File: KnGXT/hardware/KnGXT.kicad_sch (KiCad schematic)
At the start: 134 parts, among them J1 USB_C_ReceptacleUSB2.0, J2 Conn_01x10_Male, SW1 RotaryEncoder_Switch, SW10 SW_Push, SW11 SW_Push, SW12 SW_Push, SW13 SW_Push, SW14 SW_Push, SW15 SW_Push, SW16 SW_Push, SW17 SW_Push, SW2 RotaryEncoder_Switch, SW3 SW_Push, SW4 SW_Push, SW5 SW_Push, SW6 SW_Push, SW7 SW_Push, SW8 SW_Push, SW9 SW_Push, U1 AMS1117-3.3, U2 W25Q128JVS, U3 RP2040, U4 74125, Y1 12MHz

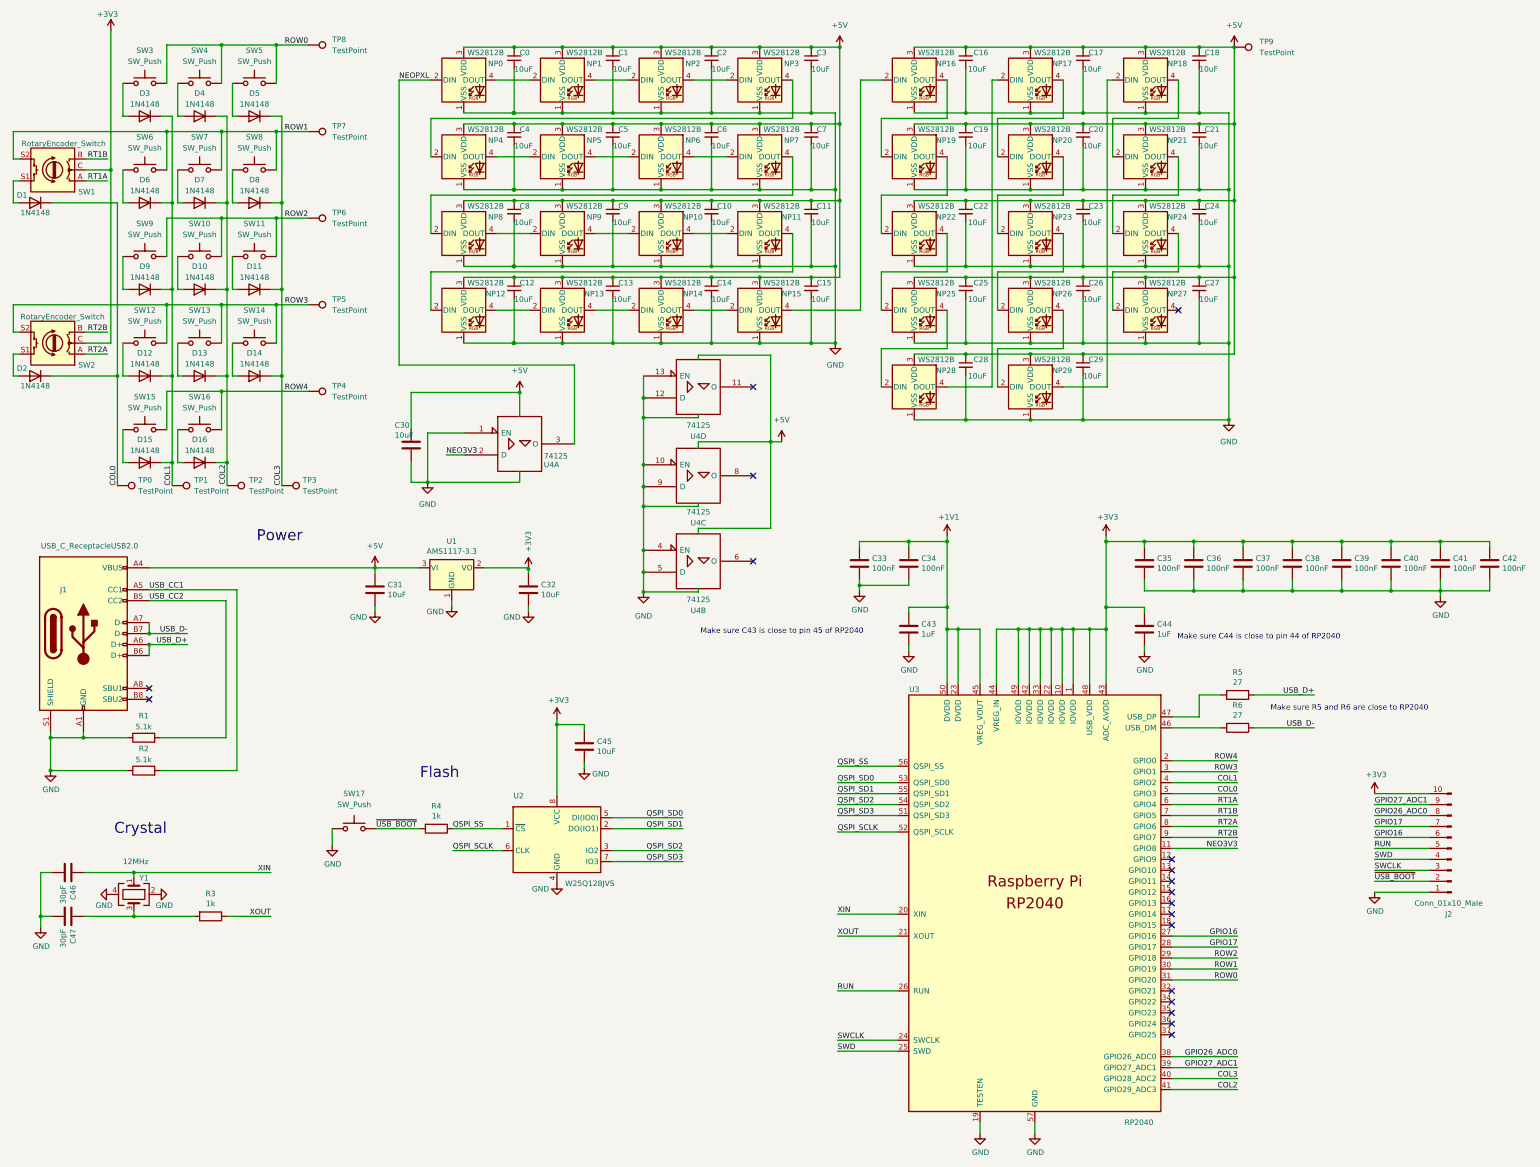
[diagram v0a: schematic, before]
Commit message: (Mostly?) update KnGXT for KiCad 7 and to use kicadlib.
KnGXT probably still needs work to pass ERC & DRC, but that's OK because any new spin of it will make further changes.
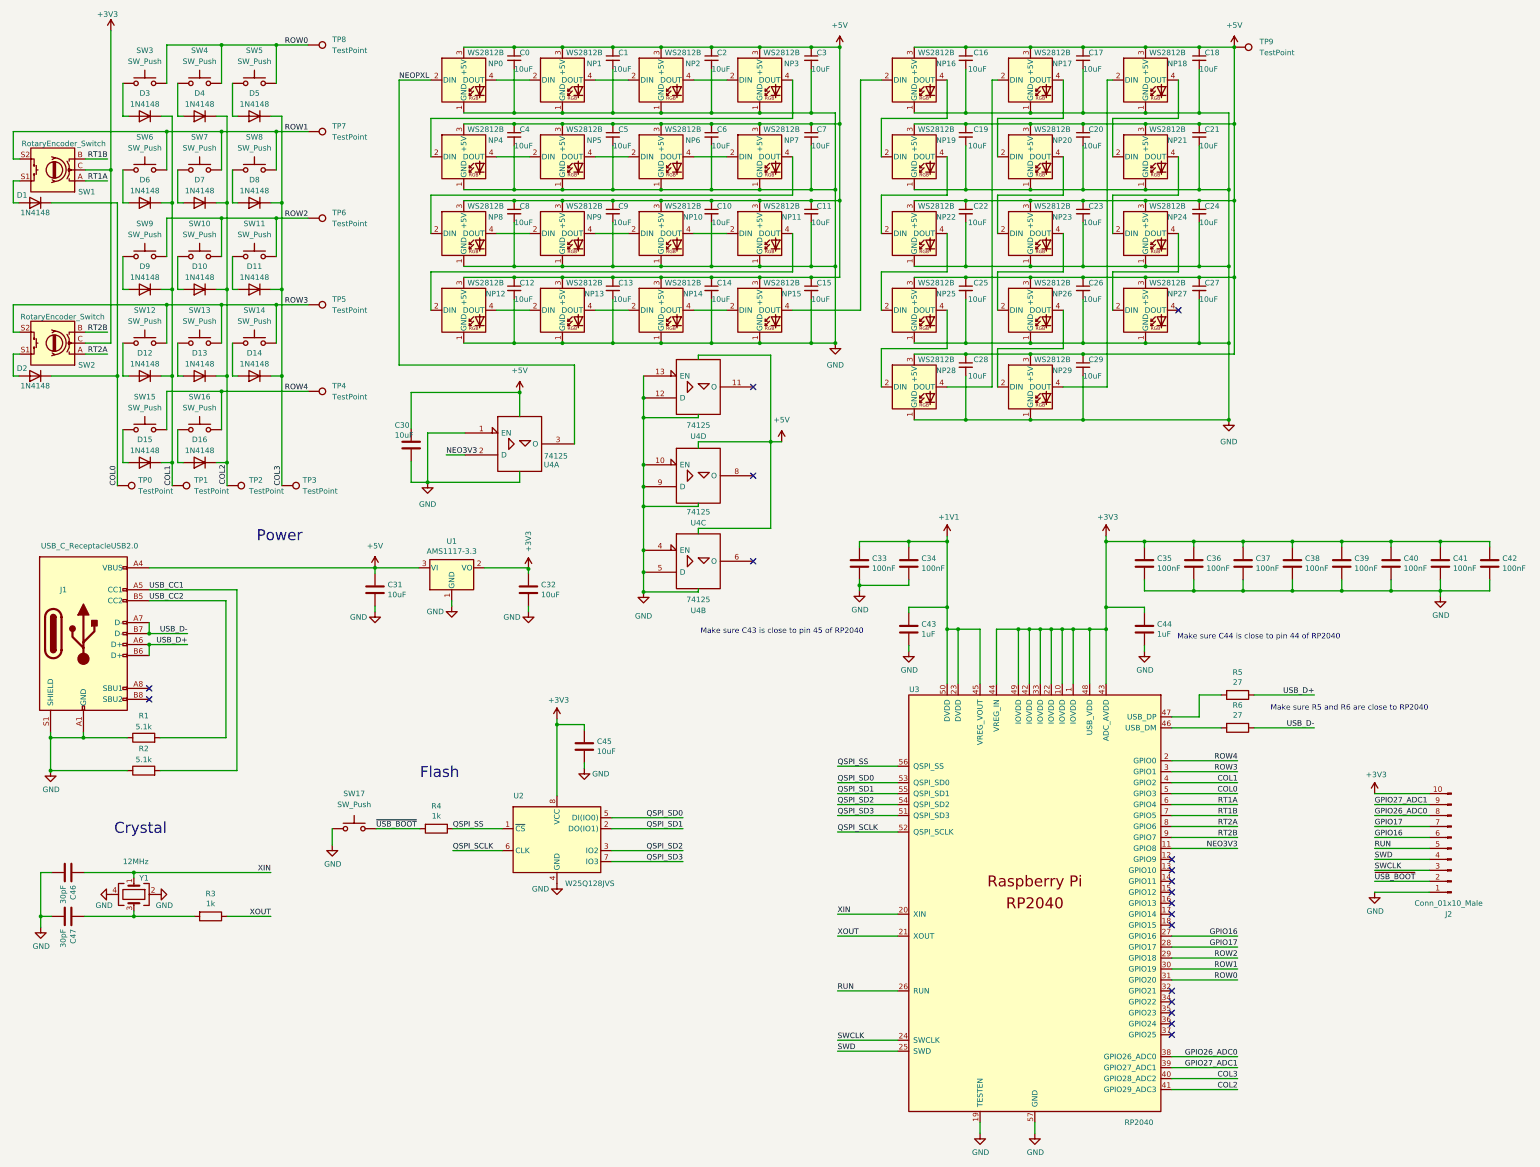
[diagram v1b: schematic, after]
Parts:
- NP0, NP1, NP10, NP11, NP12, NP13, NP14, NP15, NP16, NP17, NP18, NP19, NP2, NP20, NP21, NP22, NP23, NP24, NP25, NP26, NP27, NP28, NP29, NP3, NP4, NP5, NP6, NP7, NP8, NP9: footprint LED_SMD:LED_WS2812B_3.5x2.8_C2890364 -> Kodachi:LED XL-3528RGBW-WS2812B (3.5x2.8, C2890364); symbol LED:WS2812B_C2890364 -> Kodachi:XL-3528RGBW-WS2812B_(C2890364)
- U3: footprint RP_Silicon:RP2040-QFN-56 -> RP2040_minimal:RP2040-QFN-56; symbol RP_Silicon:RP2040 -> MCU_RaspberryPi_and_Boards:RP2040
